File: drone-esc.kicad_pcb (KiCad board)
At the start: 6 copper layers, 34 x 34 mm, 237 parts, among them J1 SM08B-SRSS-TB_LF__SN_, Q1 IRLHS6242, Q10 IRLHS6242, Q11 IRLHS6242, Q12 IRLHS6242, Q13 IRLHS6242, Q14 IRLHS6242, Q15 IRLHS6242, Q16 IRLHS6242, Q17 IRLHS6242, Q18 IRLHS6242, Q19 IRLHS6242, Q2 IRLHS6242, Q20 IRLHS6242, Q21 IRLHS6242, Q22 IRLHS6242, Q23 IRLHS6242, Q24 IRLHS6242, Q3 IRLHS6242, Q4 IRLHS6242, Q5 IRLHS6242, Q6 IRLHS6242, Q7 IRLHS6242, Q8 IRLHS6242, Q9 IRLHS6242, U10 DGD05473FNQ-7, U11 DGD05473FNQ-7, U12 AT32F421G8U7, U13 DGD05473FNQ-7, U14 DGD05473FNQ-7, U15 DGD05473FNQ-7, U16 AT32F421G8U7, U17 DGD05473FNQ-7, U18 DGD05473FNQ-7, U19 DGD05473FNQ-7, U2 INA186A3IDCKR, U20 AT32F421G8U7, U3 TLV76733DRVR, U4 TPS61023DRLR, U5 AT32F421G8U7, U6 DGD05473FNQ-7, U7 DGD05473FNQ-7, U8 DGD05473FNQ-7, U9 DGD05473FNQ-7

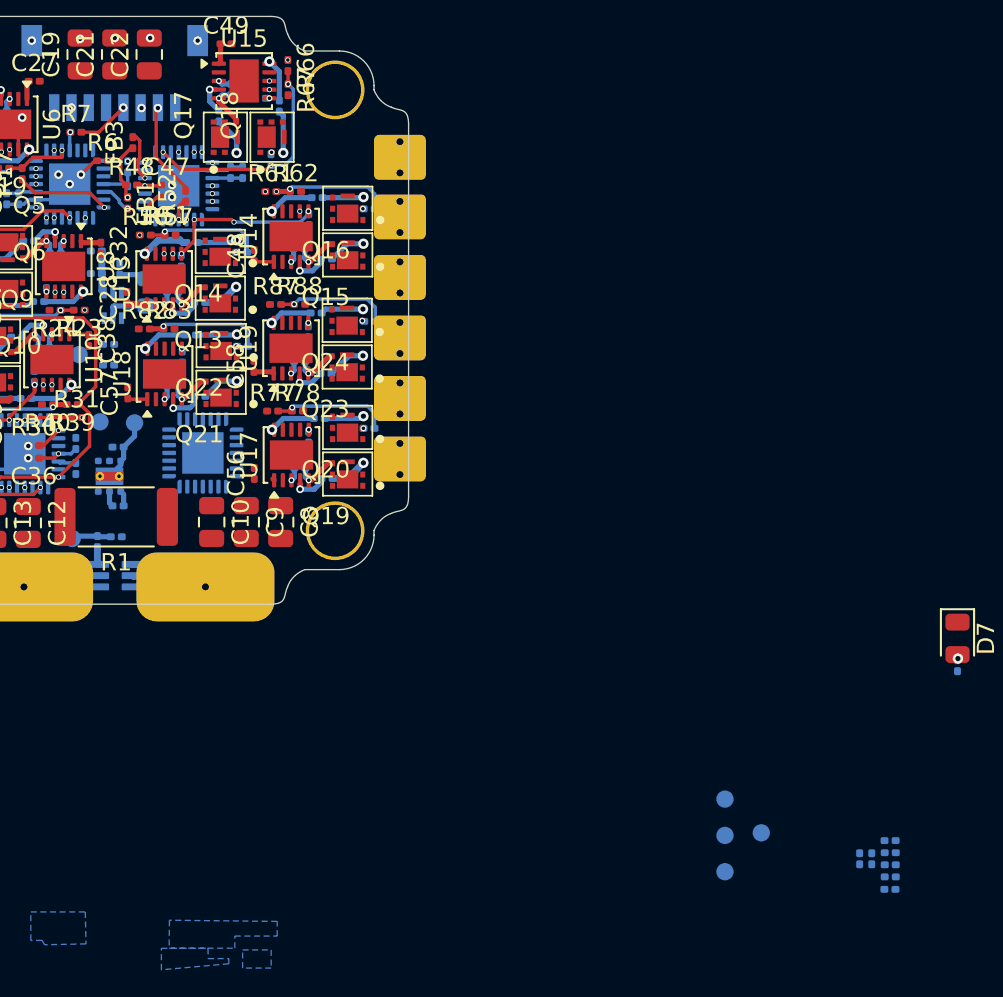
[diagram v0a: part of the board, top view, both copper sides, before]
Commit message: routed motor 4
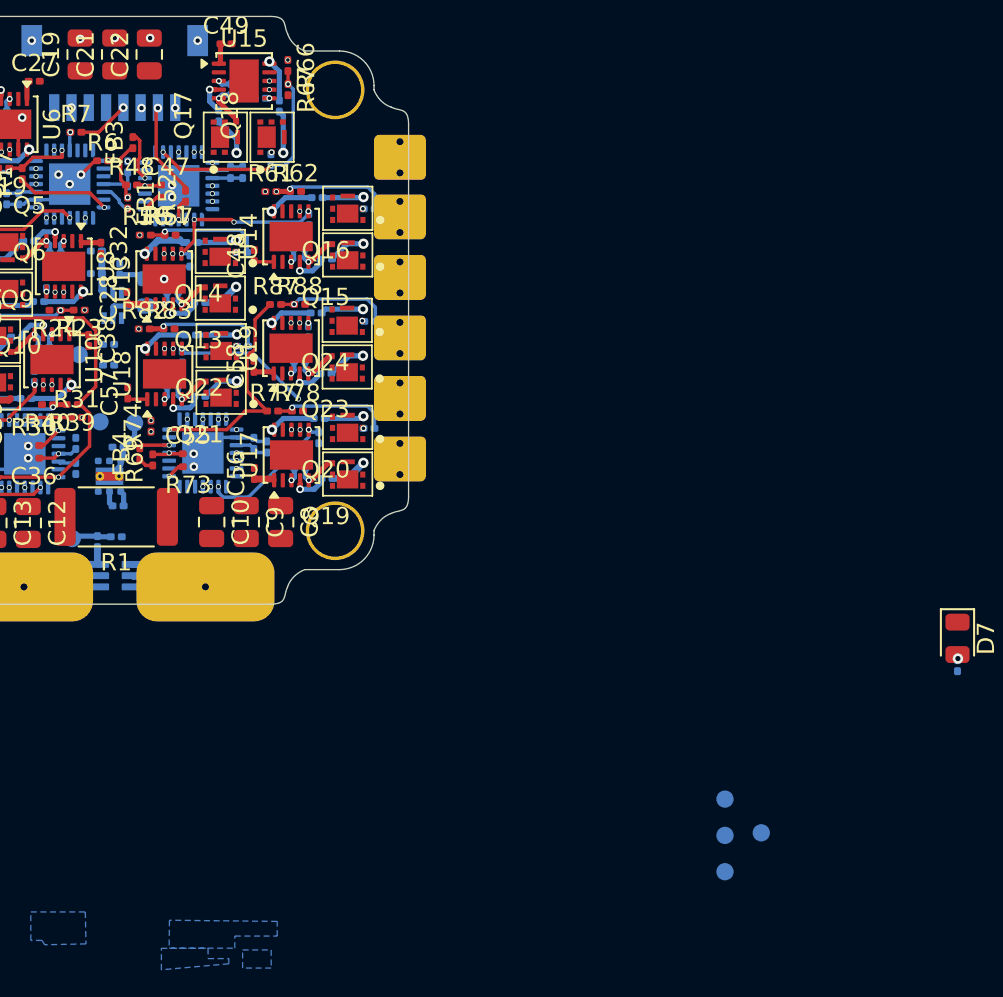
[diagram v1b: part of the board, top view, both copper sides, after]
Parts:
- C55, FB4, R69, R73, R74: moved to F.Cu
- moved R74 50.4 mm to (147.1, 101.7), turned to 90 degrees
- moved FB4 48.8 mm to (146.4, 103.3), turned to 90 degrees
- moved R69 48.7 mm to (147.2, 103.7), turned to 90 degrees
- moved R73 47.0 mm to (149.3, 104.0), turned to 180 degrees
- moved C55 46.7 mm to (149.2, 103.3), turned to 0 degrees
- moved C59 43.1 mm to (153.1, 102.7)
- moved C60 41.8 mm to (153.8, 102.9)
- moved R70 0.59 mm to (156.8, 102.4)
- moved R11 0.50 mm to (149.3, 92.2)
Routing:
- net /ESC4/ESC_EN: track 0.47 -> 24.6 mm, vias 3 -> 5
- net /ESC4/FBCOMMON: track 0.00 -> 20.1 mm, vias 0 -> 2
- net /M4: track 0.00 -> 19.8 mm, vias 0 -> 2
- net /ESC4/FBC: track 6.59 -> 17.5 mm, vias 1 -> 2
- net /ESC4/B_LOW: track 0.00 -> 9.95 mm, vias 0 -> 2
- net /ESC4/FBA: track 6.85 -> 16.8 mm, vias 1 -> 2
- net /ESC4/B_HIGH: track 0.00 -> 9.55 mm, vias 0 -> 2
- net /ESC4/C_HIGH: track 0.00 -> 7.33 mm, vias 0 -> 2
- net /ESC4/C_LOW: track 0.00 -> 7.31 mm, vias 0 -> 2
- net GND: track 28.3 -> 34.3 mm, vias 18 -> 21
- net /ESC4/FBB: track 6.91 -> 12.3 mm, vias 1 -> 3
- net /ESC4/A_HIGH: track 0.00 -> 4.97 mm, vias 0 -> 2
- net Net-(U20-PB4): track 0.00 -> 4.75 mm, vias 0 -> 2
- net /ESC4/A_LOW: track 0.00 -> 4.16 mm, vias 0 -> 2
- net +3.3V: track 8.91 -> 11.7 mm
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
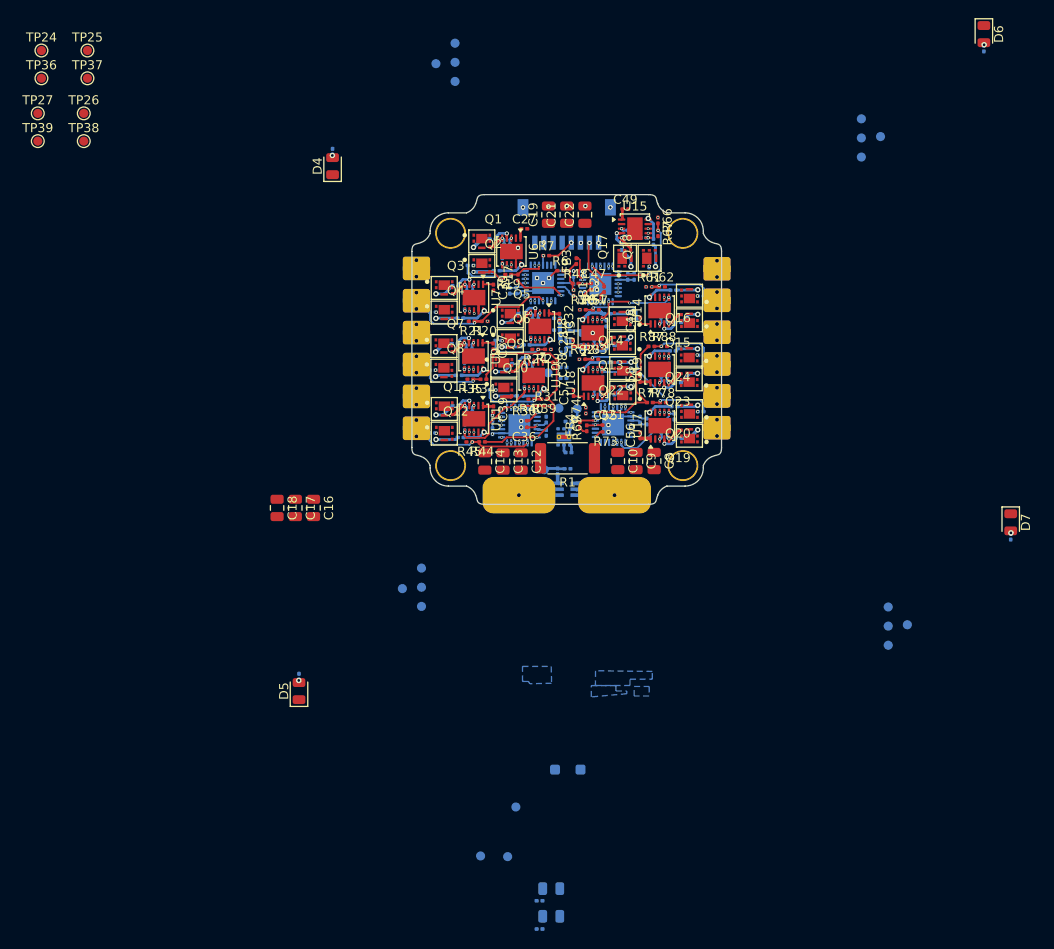
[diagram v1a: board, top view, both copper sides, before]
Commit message: routed boost converted
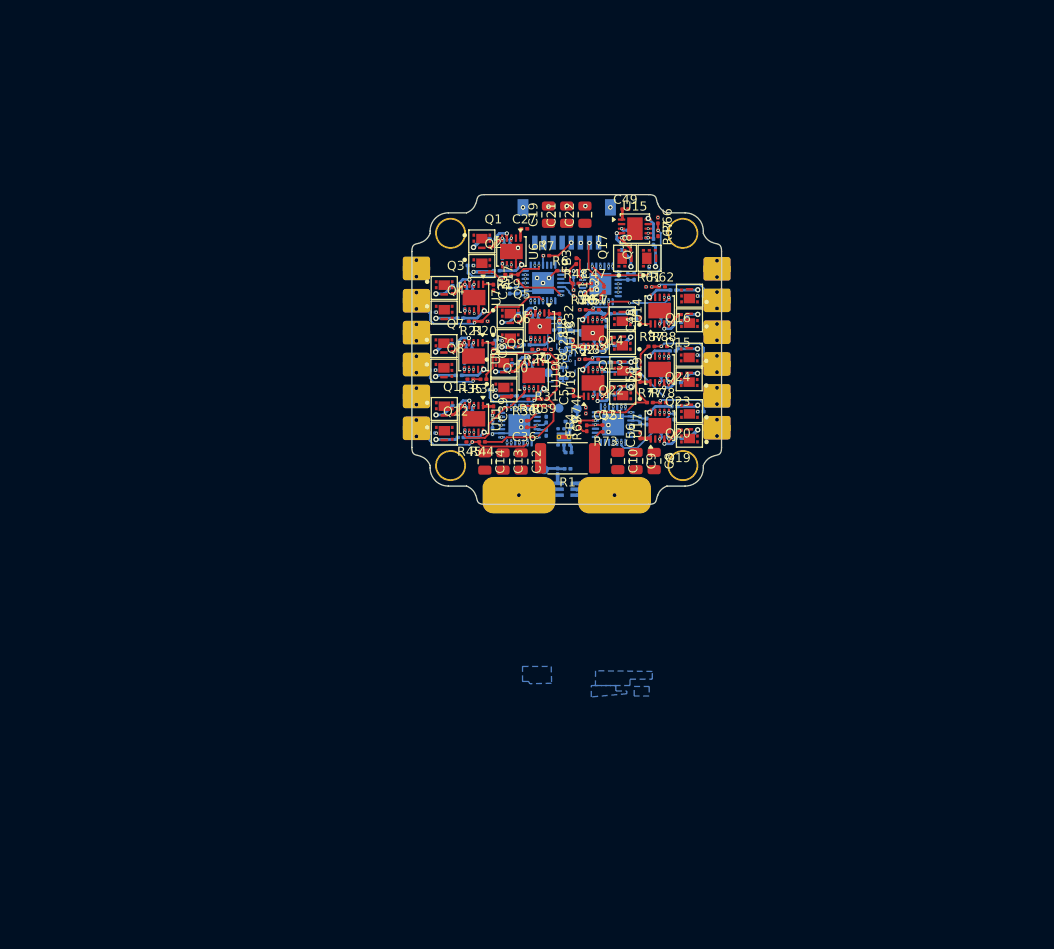
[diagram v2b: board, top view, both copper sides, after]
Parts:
- removed C16, C17, C18: 10u, Capacitor_SMD:C_0805_2012Metric
- removed D1: SMF5.0A, Diode_SMD:D_SOD-123F
- removed D2, D4, D5, D6, D7: HSMG-C170, LED_SMD:LED_0805_2012Metric
- removed D3: HSMD-C170, LED_SMD:LED_0805_2012Metric
- removed R5, R91, R92, R93, R94: 360, Resistor_SMD:R_0201_0603Metric
- removed R90: 900, Resistor_SMD:R_0201_0603Metric
- removed TP10, TP13, TP6, TP9: SWDIO, TestPoint:TestPoint_Pad_D1.0mm
- removed TP11, TP3, TP4, TP7: NRST, TestPoint:TestPoint_Pad_D1.0mm
- removed TP12, TP2, TP5, TP8: SWCLK, TestPoint:TestPoint_Pad_D1.0mm
- removed TP14: BATT, TestPoint:TestPoint_Pad_D1.0mm
- removed TP19, TP20, TP21, TP22: BOOT0, TestPoint:TestPoint_Pad_D1.0mm
- removed TP23: GND, TestPoint:TestPoint_Pad_D1.0mm
- removed TP24, TP25, TP26, TP27: GAH, TestPoint:TestPoint_Pad_D1.0mm
- removed TP28: 3V3, TestPoint:TestPoint_Pad_D1.0mm
- removed TP36, TP37, TP38, TP39: GAL, TestPoint:TestPoint_Pad_D1.0mm
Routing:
- net GND: track 34.3 -> 36.2 mm, vias 21 -> 26
- net Net-(D4-A): track 0.24 -> 0.00 mm, vias 1 -> 0
- net Net-(D7-A): track 0.24 -> 0.00 mm, vias 1 -> 0
- net Net-(D5-A): track 0.24 -> 0.00 mm, vias 1 -> 0
- net Net-(D6-A): track 0.24 -> 0.00 mm, vias 1 -> 0

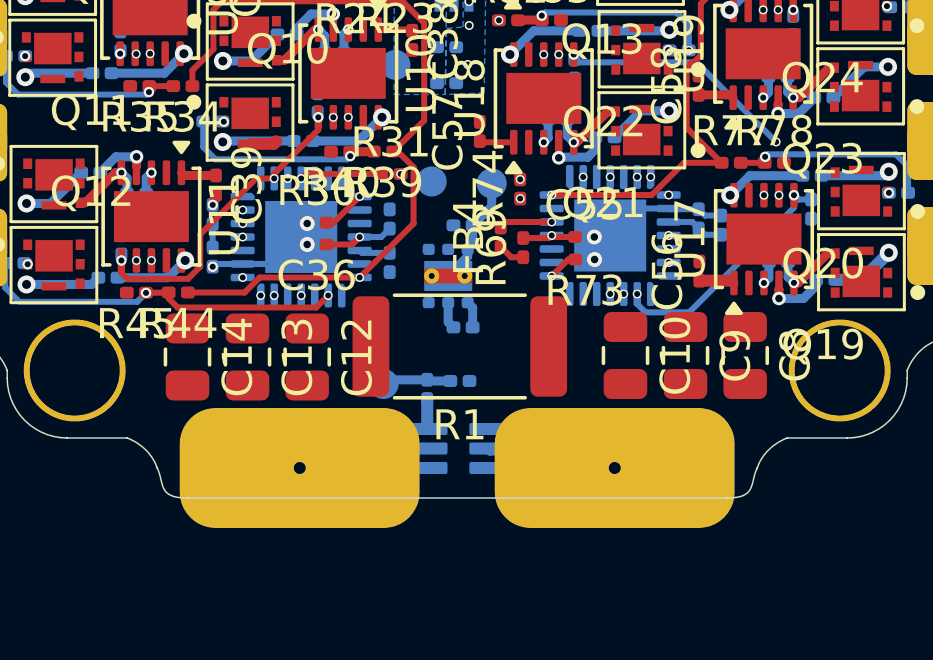
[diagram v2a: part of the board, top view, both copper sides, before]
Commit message: routed ldo and ina
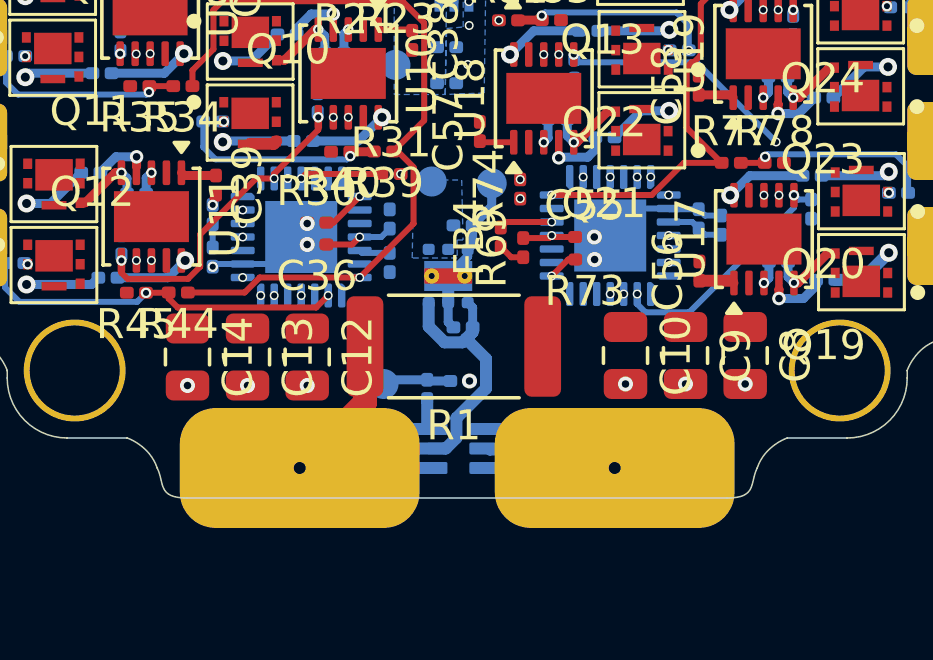
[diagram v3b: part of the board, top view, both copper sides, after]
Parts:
- moved R1 0.20 mm to (144.9, 107.0)
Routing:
- net /VBAT_IN: track 0.00 -> 9.28 mm
- net +BATT: track 2.49 -> 10.3 mm
- net GND: track 36.2 -> 40.4 mm, vias 26 -> 33
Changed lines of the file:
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@@
 	(footprint "Resistor_SMD:R_2512_6332Metric"
 		(layer "F.Cu")
-		(at 145.0875 106.95 180)
+		(at 144.8875 106.95 180)
 		(descr "Resistor SMD 2512 (6332 Metric), square (rectangular) end terminal, IPC-7351 nominal, (Body size source: IPC-SM-782 page 72, https://www.pcb-3d.com/wordpress/wp-content/uploads/ipc-sm-782a_amendment_1_and_2.pdf)")
 		(tags "resistor")
@@
 	)
 	(via
+		(at 152.61 108.2)
+		(size 0.5)
+		(drill 0.25)
+		(layers "F.Cu" "B.Cu")
+		(net "GND")
+	)
+	(via
 		(at 145.35 97.55)
 		(size 0.3)
@@
 	)
 	(via
+		(at 140 108.25)
+		(size 0.5)
+		(drill 0.25)
+		(layers "F.Cu" "B.Cu")
+		(net "GND")
+	)
+	(via
+		(at 154.6 108.2)
+		(size 0.5)
+		(drill 0.25)
+		(layers "F.Cu" "B.Cu")
+		(net "GND")
+	)
+	(via
 		(at 142.4 87.7)
 		(size 0.5)
@@
 	)
 	(via
+		(at 136.01 108.25)
+		(size 0.5)
+		(drill 0.25)
+		(layers "F.Cu" "B.Cu")
+		(net "GND")
+	)
+	(via
 		(at 140 102.85)
 		(size 0.5)
@@
 	)
 	(via
+		(at 138.01 108.25)
+		(size 0.5)
+		(drill 0.25)
+		(layers "F.Cu" "B.Cu")
+		(net "GND")
+	)
+	(via
 		(at 140 103.55)
 		(size 0.5)
@@
 	)
 	(via
+		(at 150.61 108.2)
+		(size 0.5)
+		(drill 0.25)
+		(layers "F.Cu" "B.Cu")
+		(net "GND")
+	)
+	(via
 		(at 142.5 83.275)
 		(size 0.5)
@@
 	)
 	(via
+		(at 145.41 108.1)
+		(size 0.5)
+		(drill 0.25)
+		(layers "F.Cu" "B.Cu")
+		(net "GND")
+	)
+	(via
 		(at 136.85 104.29)
 		(size 0.35)
@@
 	)
 	(segment
+		(start 144.7 105.4875)
+		(end 144.7 104.6)
+		(width 0.4)
+		(layer "B.Cu")
+		(net "GND")
+	)
+	(segment
 		(start 139.45 88.87)
 		(end 138.75 88.87)
@@
 	)
 	(segment
+		(start 149.685 110.435)
+		(end 150.25 111)
+		(width 0.4)
+		(layer "B.Cu")
+		(net "GND")
+	)
+	(segment
 		(start 145.35 103.7125)
 		(end 145.35 103.95)
@@
 	)
 	(segment
+		(start 147.245 110.435)
+		(end 149.685 110.435)
+		(width 0.4)
+		(layer "B.Cu")
+		(net "GND")
+	)
+	(segment
 		(start 146.15 101.5125)
 		(end 146.15 102.2775)
@@
 	)
 	(segment
+		(start 144.576544 106.8125)
+		(end 144.05 106.285956)
+		(width 0.4)
+		(layer "B.Cu")
+		(net "+BATT")
+	)
+	(segment
 		(start 145.515 105.6525)
 		(end 145.515 106.3125)
@@
 	)
 	(segment
+		(start 144.62136 110.35)
+		(end 144.08 110.35)
+		(width 0.4)
+		(layer "B.Cu")
+		(net "+BATT")
+	)
+	(segment
+		(start 144.05 106.285956)
+		(end 144.05 105.4875)
+		(width 0.4)
+		(layer "B.Cu")
+		(net "+BATT")
+	)
+	(segment
+		(start 145.173456 106.8125)
+		(end 144.576544 106.8125)
+		(width 0.4)
+		(layer "B.Cu")
+		(net "+BATT")
+	)
+	(segment
+		(start 145.515 106.3125)
+		(end 145.515 106.470956)
+		(width 0.4)
+		(layer "B.Cu")
+		(net "+BATT")
+	)
+	(segment
+		(start 144.975 109.333456)
+		(end 144.975 109.99636)
+		(width 0.4)
+		(layer "B.Cu")
+		(net "+BATT")
+	)
+	(segment
+		(start 145.292978 106.692978)
+		(end 145.96 107.36)
+		(width 0.4)
+		(layer "B.Cu")
+		(net "+BATT")
+	)
+	(segment
+		(start 145.292978 106.692978)
+		(end 145.173456 106.8125)
+		(width 0.4)
+		(layer "B.Cu")
+		(net "+BATT")
+	)
+	(segment
+		(start 144.975 109.99636)
+		(end 144.62136 110.35)
+		(width 0.4)
+		(layer "B.Cu")
+		(net "+BATT")
+	)
+	(segment
+		(start 145.96 108.348456)
+		(end 144.975 109.333456)
+		(width 0.4)
+		(layer "B.Cu")
+		(net "+BATT")
+	)
+	(segment
+		(start 145.96 107.36)
+		(end 145.96 108.348456)
+		(width 0.4)
+		(layer "B.Cu")
+		(net "+BATT")
+	)
+	(segment
 		(start 145.292498 92.937499)
 		(end 146.554997 92.937499)
@@
 		(net "+BATT")
 	)
+	(segment
+		(start 145.515 106.470956)
+		(end 145.292978 106.692978)
+		(width 0.4)
+		(layer "B.Cu")
+		(net "+BATT")
+	)
 	(via
 		(at 152.065002 99.094998)
@@
 	)
 	(segment
+		(start 139.75 111)
+		(end 141.925 108.825)
+		(width 0.8)
+		(layer "F.Cu")
+		(net "/VBAT_IN")
+	)
+	(segment
+		(start 141.925 108.825)
+		(end 141.925 106.95)
+		(width 0.8)
+		(layer "F.Cu")
+		(net "/VBAT_IN")
+	)
+	(segment
+		(start 144.08 111)
+		(end 139.75 111)
+		(width 0.4)
+		(layer "B.Cu")
+		(net "/VBAT_IN")
+	)
+	(segment
 		(start 141.05 90.995)
 		(end 140.85 90.995)
@@
 		)
 		(min_thickness 0.15)
-		(fill yes
+		(fill
 			(thermal_gap 0.2)
 			(thermal_bridge_width 0.3)
@@
 		)
 		(min_thickness 0.15)
-		(fill yes
+		(fill
 			(thermal_gap 0.2)
 			(thermal_bridge_width 0.3)
@@
 		)
 		(min_thickness 0.15)
-		(fill yes
+		(fill
 			(thermal_gap 0.2)
 			(thermal_bridge_width 0.3)
@@
 		)
 		(min_thickness 0.15)
-		(fill yes
+		(fill
 			(thermal_gap 0.2)
 			(thermal_bridge_width 0.3)
@@
 		)
 		(min_thickness 0.15)
-		(fill yes
+		(fill
 			(thermal_gap 0.2)
 			(thermal_bridge_width 0.3)
@@
 	)
 	(zone
+		(net "+3.3V")
+		(layer "B.Cu")
+		(hatch edge 0.5)
+		(priority 8)
+		(connect_pads
+			(clearance 0.2)
+		)
+		(min_thickness 0.15)
+		(fill
+			(thermal_gap 0.2)
+			(thermal_bridge_width 0.3)
+			(island_removal_mode 0)
+		)
+		(polygon
+			(pts
+				(xy 143.55 101.4) (xy 145.15 101.4) (xy 145.195 103.4) (xy 145 103.4) (xy 145 104) (xy 143.5 104)
+			)
+		)
+	)
+	(zone
 		(net "+BATT")
 		(layer "B.Cu")
@@
 		)
 		(min_thickness 0.15)
-		(fill yes
+		(fill
 			(thermal_gap 0.2)
 			(thermal_bridge_width 0.3)
@@
 		)
 		(min_thickness 0.15)
-		(fill yes
+		(fill
 			(thermal_gap 0.2)
 			(thermal_bridge_width 0.3)
@@
 		)
 		(min_thickness 0.15)
-		(fill yes
+		(fill
 			(thermal_gap 0.2)
 			(thermal_bridge_width 0.3)
@@
 		)
 		(min_thickness 0.15)
-		(fill yes
+		(fill
 			(thermal_gap 0.2)
 			(thermal_bridge_width 0.3)

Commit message: finish before power
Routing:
- net +BATT: vias 0 -> 7
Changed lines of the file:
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@@
 		(net "/ESC2/FBB")
+	)
+	(via
+		(at 154.6 106.3)
+		(size 0.5)
+		(drill 0.25)
+		(layers "F.Cu" "B.Cu")
+		(net "+BATT")
+	)
+	(via
+		(at 138.01 106.35)
+		(size 0.5)
+		(drill 0.25)
+		(layers "F.Cu" "B.Cu")
+		(net "+BATT")
+	)
+	(via
+		(at 152.61 106.3)
+		(size 0.5)
+		(drill 0.25)
+		(layers "F.Cu" "B.Cu")
+		(net "+BATT")
+	)
+	(via
+		(at 150.61 106.3)
+		(size 0.5)
+		(drill 0.25)
+		(layers "F.Cu" "B.Cu")
+		(net "+BATT")
+	)
+	(via
+		(at 136.01 106.35)
+		(size 0.5)
+		(drill 0.25)
+		(layers "F.Cu" "B.Cu")
+		(net "+BATT")
+	)
+	(via
+		(at 140 106.35)
+		(size 0.5)
+		(drill 0.25)
+		(layers "F.Cu" "B.Cu")
+		(net "+BATT")
+	)
+	(via
+		(at 147.85 106.95)
+		(size 0.5)
+		(drill 0.25)
+		(layers "F.Cu" "B.Cu")
+		(net "+BATT")
 	)
 	(segment
